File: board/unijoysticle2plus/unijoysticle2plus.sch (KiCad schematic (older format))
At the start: 24 parts, among them J1 DB9_Female, J2 DB9_Female, J3 Barrel_Jack, J4 Conn_01x02_Male, SW1 SW_Push, SW2 SW_SPST, SW3 SW_Push, SW4 SW_Push, U1 ESP32-WROOM-32D, U2 74LS05, U3 74LS05

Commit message: unijoysticle 2 plus: WIP
testing with different LDO, USB connectors... still very much WIP
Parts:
- removed C? (x2): 4.7uF, symbol Device:C_Small
- removed J4: Conn_01x02_Male, Connector_PinHeader_2.54mm:PinHeader_1x02_P2.54mm_Vertical, symbol Connector:Conn_01x02_Male
- removed U?: AP2114H-3_3TRG1, digikey-footprints:SOT-223, symbol dk_PMIC-Voltage-Regulators-Linear:AP2114H-3_3TRG1
- added C? (x3): 4.7uF, symbol Device:C_Small
- added C?: 0.1uF, symbol Device:C_Small
- added D? (x3): ESD9B5.0ST5G, Diode_SMD:D_SOD-923, symbol Diode:ESD9B5.0ST5G
- added D?: 1N5819, Diode_THT:D_DO-41_SOD81_P10.16mm_Horizontal, symbol Diode:1N5819
- added J?: Conn_01x03_Male, symbol Connector:Conn_01x03_Male
- added Q?: S8050, Package_TO_SOT_THT:TO-92_Inline, symbol Transistor_BJT:S8050
- added U?: AP2114H-3_3TRG1, digikey-footprints:SOT-223, symbol dk_PMIC-Voltage-Regulators-Linear:AP2114H-3_3TRG1
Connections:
- net labels added: GPIO04, USB_DN, USB_DP, VBUS
- net labels removed: +3.3V
- wire segments 129 -> 166
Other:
- moved on the sheet: C1, D3, D4, J1, J2, J3, J?, R3, SW2, SW3, SW4, U1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

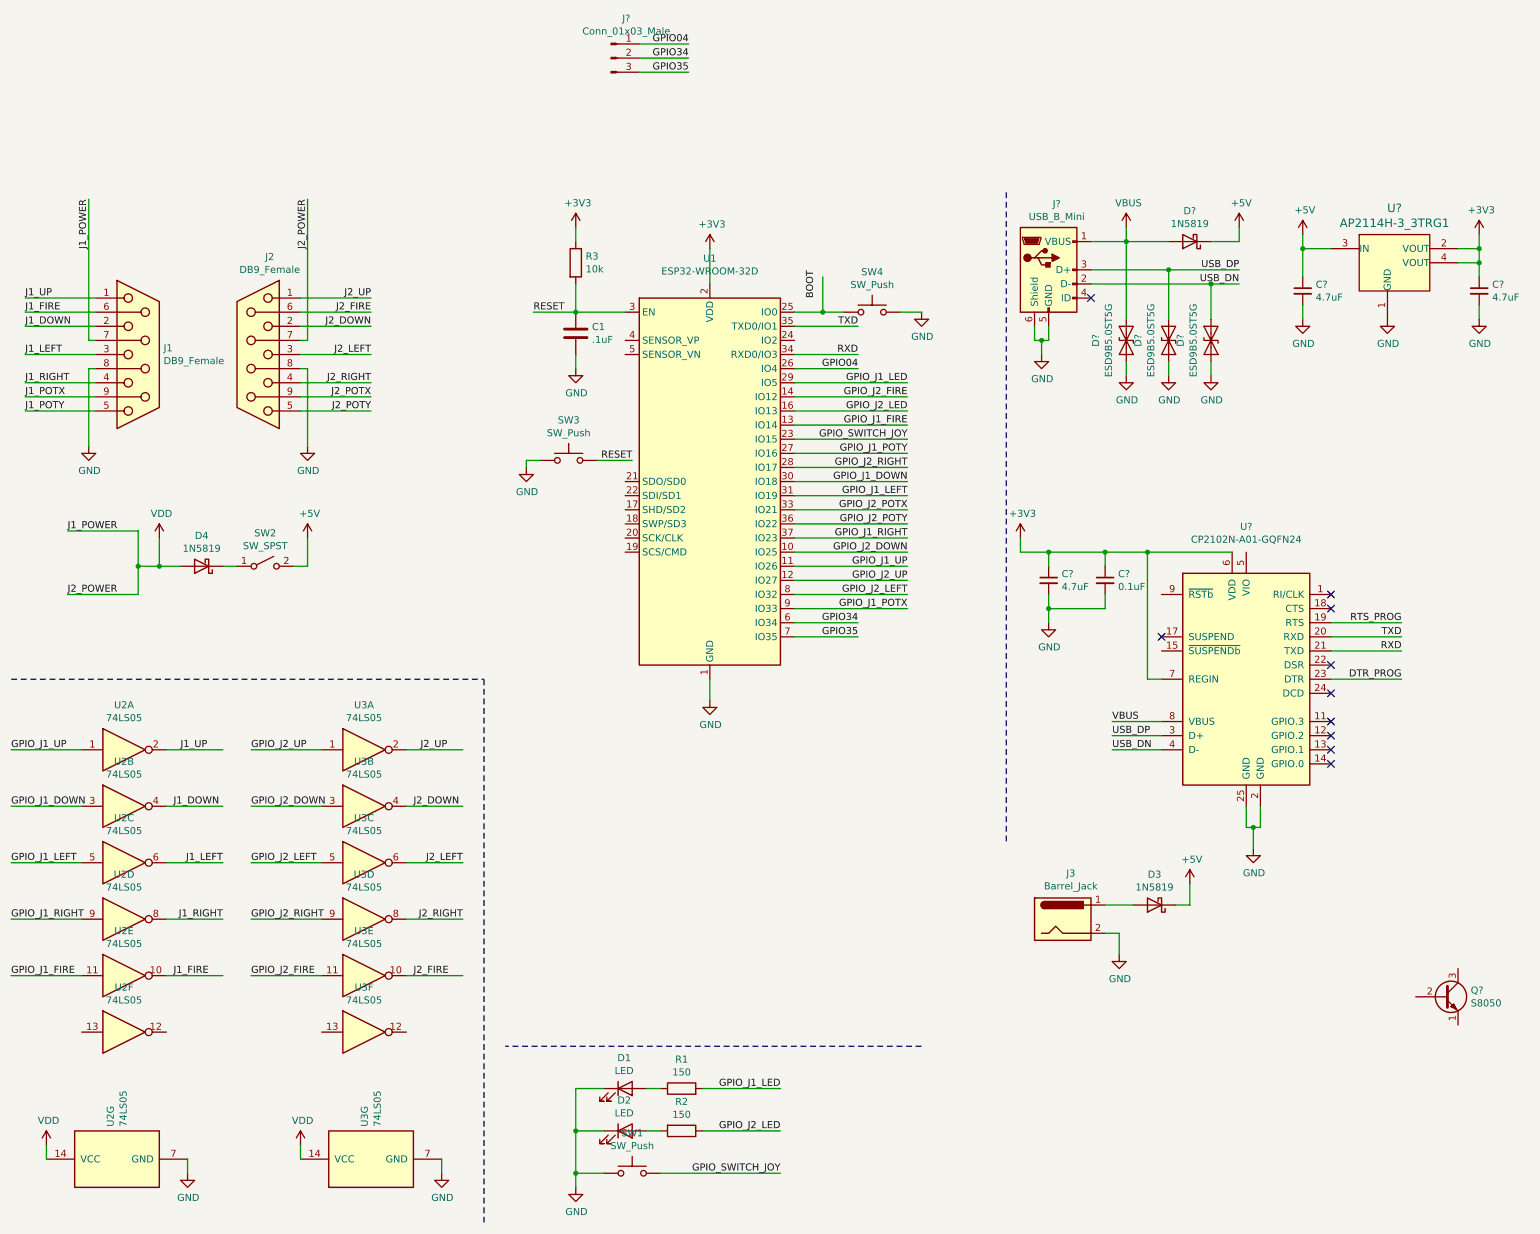
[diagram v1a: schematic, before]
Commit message: unijoysticle 2 plus:
usb micro instead of mini
connect transistors for auto-prog
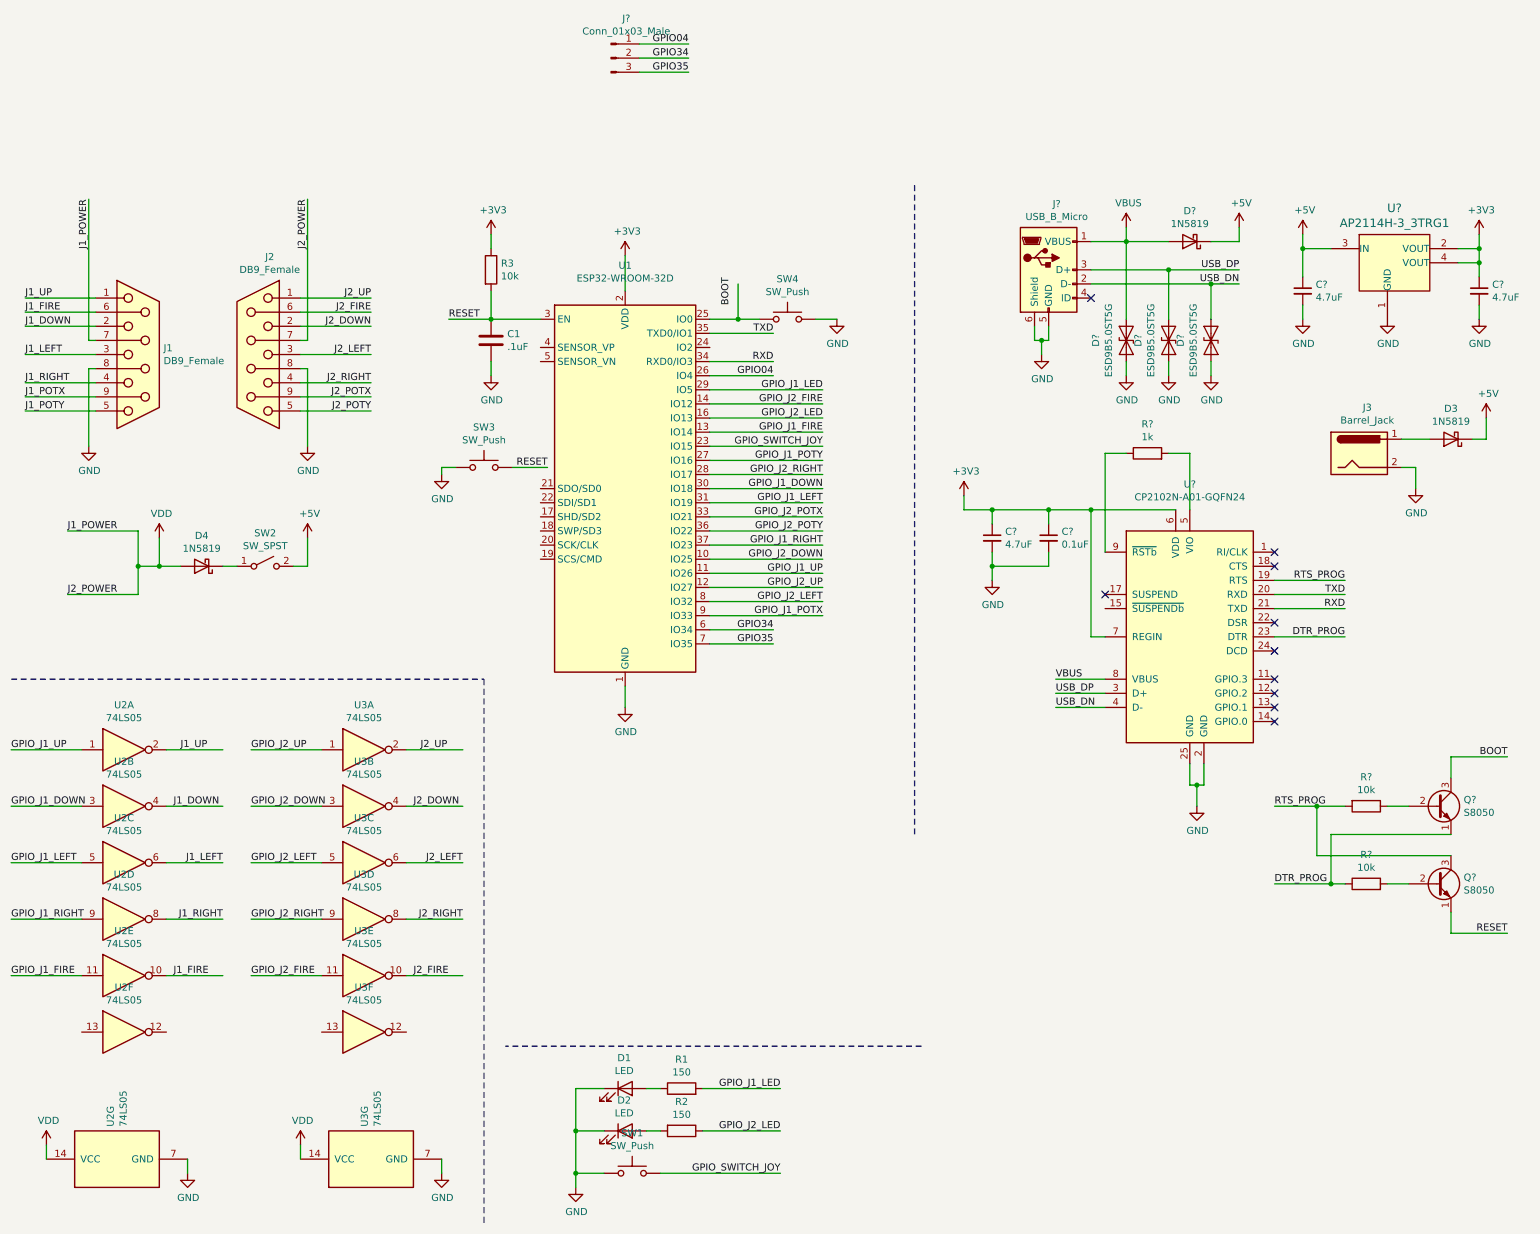
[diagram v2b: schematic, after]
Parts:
- removed J?: USB_B_Mini, symbol Connector:USB_B_Mini
- added J?: USB_B_Micro, symbol Connector:USB_B_Micro
- added Q?: S8050, Package_TO_SOT_THT:TO-92_Inline, symbol Transistor_BJT:S8050
- added R?: 1k, symbol Device:R
- added R? (x2): 10k, symbol Device:R
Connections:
- wire segments 166 -> 184
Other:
- moved on the sheet: C1, C?, D3, J3, Q?, R3, SW3, SW4, U1, U?

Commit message: unijoysticle2plus: add some footprints
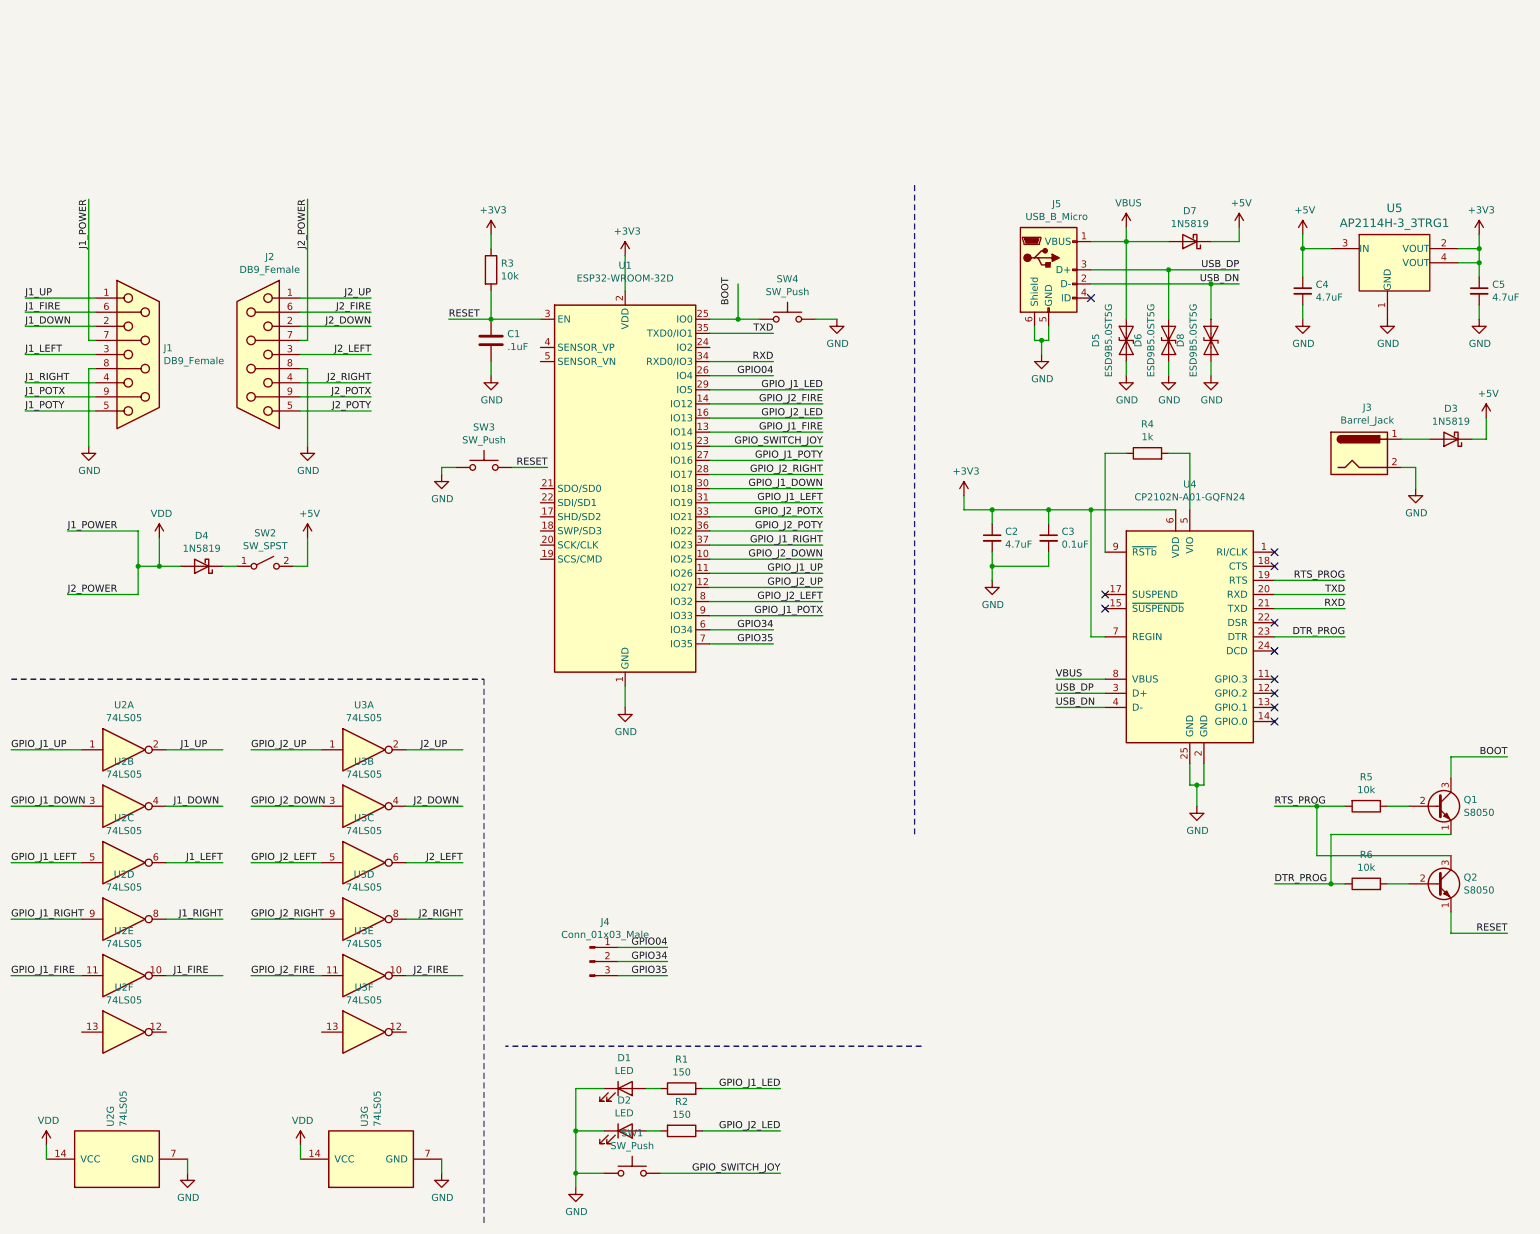
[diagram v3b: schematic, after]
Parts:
- removed U?: AP2114H-3_3TRG1, digikey-footprints:SOT-223, symbol dk_PMIC-Voltage-Regulators-Linear:AP2114H-3_3TRG1
- added U5: AP2114H-3_3TRG1, Package_TO_SOT_SMD:SOT-223, symbol dk_PMIC-Voltage-Regulators-Linear:AP2114H-3_3TRG1
- J3: footprint (none) -> Connector_BarrelJack:BarrelJack_Horizontal
- J5: renamed from J?; footprint (none) -> Connectors:USB-MICROB
- R1, R2, R3: footprint (none) -> Resistor_SMD:R_0805_2012Metric_Pad1.20x1.40mm_HandSolder
- R4, R5, R6: renamed from R?; footprint (none) -> Resistor_SMD:R_0805_2012Metric_Pad1.20x1.40mm_HandSolder
- U1: footprint digikey-footprints:ESP32-WROOM-32D -> RF_Module:ESP32-WROOM-32
- U2, U3: footprint (none) -> Silicon-Standard:SO14
- gave numbers to parts that had none: 12
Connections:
- no-connect marks 10 -> 11
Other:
- moved on the sheet: J4
